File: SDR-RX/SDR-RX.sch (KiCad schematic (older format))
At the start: 44 parts, among them J1 Program, J2 Vin, J3 FM Antenna, J4 AM Antenna, J5 Conn_01x03_Male, Q1 S8050, Q2 S8050, SW1 Reset ESP, SW2 3V3 J5/J2, U1 Si4734-D60-GU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

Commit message: PCB layout for plastic enclosure
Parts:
- added H1, H2, H3, H4: MountingHole_Pad, MountingHole:MountingHole_2.7mm_Pad_Via, symbol Mechanical:MountingHole_Pad
- added J6: GPS, Connector_JST:JST_SH_BM04B-SRSS-TB_1x04-1MP_P1.00mm_Vertical, symbol Connector:Conn_01x04_Male
- J2: footprint Connector_JST:JST_XH_S2B-XH-A-1_1x02_P2.50mm_Horizontal -> Connector_JST:JST_XH_B2B-XH-A_1x02_P2.50mm_Vertical
- J4: footprint Connector_Coaxial:SMA_Samtec_SMA-J-P-X-ST-EM1_EdgeMount -> Connector_Coaxial:SMB_Jack_Vertical
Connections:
- net +3V3: now also J6.4 (Pin_4)
- net GND: now also J6.1 (Pin_1)
- net at U2.24 (IO2): now also J6.3 (Pin_3)
- net at U2.26 (IO4): now also J6.2 (Pin_2)
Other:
- note added: "ESP RX/GPS TX"
- note added: "ESP TX/GPS RX"
- moved on the sheet: J5
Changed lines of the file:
@@
 L power:GND #PWR0103
 U 1 1 5FE984E0
-P 6000 4200
-F 0 "#PWR0103" H 6000 3950 50  0001 C CNN
-F 1 "GND" H 6000 4000 50  0000 C CNN
-F 2 "" H 6000 4200 50  0001 C CNN
-F 3 "" H 6000 4200 50  0001 C CNN
-	1    6000 4200
+P 10050 1800
+F 0 "#PWR0103" H 10050 1550 50  0001 C CNN
+F 1 "GND" H 10050 1600 50  0000 C CNN
+F 2 "" H 10050 1800 50  0001 C CNN
+F 3 "" H 10050 1800 50  0001 C CNN
+	1    10050 1800
 	1    0    0    -1
 $EndComp
@@
 L power:GND1 #RFGND0102
 U 1 1 6006F2B5
-P 6200 4200
-F 0 "#RFGND0102" H 6200 3950 50  0001 C CNN
-F 1 "GND1" H 6100 4000 50  0000 L CNN
-F 2 "" H 6200 4200 50  0001 C CNN
-F 3 "" H 6200 4200 50  0001 C CNN
-	1    6200 4200
+P 10250 1800
+F 0 "#RFGND0102" H 10250 1550 50  0001 C CNN
+F 1 "GND1" H 10150 1600 50  0000 L CNN
+F 2 "" H 10250 1800 50  0001 C CNN
+F 3 "" H 10250 1800 50  0001 C CNN
+	1    10250 1800
 	1    0    0    -1
 $EndComp
@@
 F 0 "J2" H 5042 2225 50  0000 C CNN
 F 1 "Vin " H 5042 2316 50  0000 C CNN
-F 2 "Connector_JST:JST_XH_S2B-XH-A-1_1x02_P2.50mm_Horizontal" H 5150 2550 50  0001 C CNN
+F 2 "Connector_JST:JST_XH_B2B-XH-A_1x02_P2.50mm_Vertical" H 5150 2550 50  0001 C CNN
 F 3 "~" H 5150 2550 50  0001 C CNN
 	1    5150 2550
@@
 L Connector:Conn_01x03_Male J5
 U 1 1 6056D8FD
-P 6000 3700
-F 0 "J5" V 6062 3844 50  0000 L CNN
-F 1 "Conn_01x03_Male" V 6153 3844 50  0000 L CNN
-F 2 "Connector_PinHeader_2.54mm:PinHeader_1x03_P2.54mm_Vertical" H 6000 3700 50  0001 C CNN
-F 3 "~" H 6000 3700 50  0001 C CNN
-	1    6000 3700
+P 10050 1300
+F 0 "J5" V 10112 1444 50  0000 L CNN
+F 1 "Conn_01x03_Male" V 10203 1444 50  0000 L CNN
+F 2 "Connector_PinHeader_2.54mm:PinHeader_1x03_P2.54mm_Vertical" H 10050 1300 50  0001 C CNN
+F 3 "~" H 10050 1300 50  0001 C CNN
+	1    10050 1300
 	0    1    1    0
 $EndComp
 Wire Wire Line
-	5900 3900 6000 3900
-Wire Wire Line
-	6100 3900 6000 3900
-Connection ~ 6000 3900
+	9950 1500 10050 1500
+Wire Wire Line
+	10150 1500 10050 1500
+Connection ~ 10050 1500
 $Comp
 L Transistor_BJT:S8050 Q2
@@
 F 0 "J4" H 6850 5375 50  0000 L CNN
 F 1 "AM Antenna" H 6850 5284 50  0000 L CNN
-F 2 "Connector_Coaxial:SMA_Samtec_SMA-J-P-X-ST-EM1_EdgeMount" H 6750 5400 50  0001 C CNN
+F 2 "Connector_Coaxial:SMB_Jack_Vertical" H 6750 5400 50  0001 C CNN
 F 3 " ~" H 6750 5400 50  0001 C CNN
 	1    6750 5400
@@
 Connection ~ 7900 2050
 Wire Wire Line
-	6000 4200 6000 4150
-Wire Wire Line
-	6000 4150 6200 4150
-Wire Wire Line
-	6200 4150 6200 4200
-Wire Wire Line
-	6000 4150 6000 3900
-Connection ~ 6000 4150
+	10050 1800 10050 1750
+Wire Wire Line
+	10050 1750 10250 1750
+Wire Wire Line
+	10250 1750 10250 1800
+Wire Wire Line
+	10050 1750 10050 1500
+Connection ~ 10050 1750
 Wire Wire Line
 	5600 1000 5600 1150
@@
 Wire Wire Line
 	5600 1150 5600 1400
+$Comp
+L Mechanical:MountingHole_Pad H1
+U 1 1 6093FE17
+P 8500 1250
+F 0 "H1" H 8600 1299 50  0000 L CNN
+F 1 "MountingHole_Pad" H 8600 1208 50  0000 L CNN
+F 2 "MountingHole:MountingHole_2.7mm_Pad_Via" H 8500 1250 50  0001 C CNN
+F 3 "~" H 8500 1250 50  0001 C CNN
+	1    8500 1250
+	1    0    0    -1
+$EndComp
+$Comp
+L Mechanical:MountingHole_Pad H2
+U 1 1 6096087A
+P 8500 1550
+F 0 "H2" H 8600 1599 50  0000 L CNN
+F 1 "MountingHole_Pad" H 8600 1508 50  0000 L CNN
+F 2 "MountingHole:MountingHole_2.7mm_Pad_Via" H 8500 1550 50  0001 C CNN
+F 3 "~" H 8500 1550 50  0001 C CNN
+	1    8500 1550
+	1    0    0    -1
+$EndComp
+$Comp
+L Mechanical:MountingHole_Pad H3
+U 1 1 6096136C
+P 8500 1850
+F 0 "H3" H 8600 1899 50  0000 L CNN
+F 1 "MountingHole_Pad" H 8600 1808 50  0000 L CNN
+F 2 "MountingHole:MountingHole_2.7mm_Pad_Via" H 8500 1850 50  0001 C CNN
+F 3 "~" H 8500 1850 50  0001 C CNN
+	1    8500 1850
+	1    0    0    -1
+$EndComp
+$Comp
+L Mechanical:MountingHole_Pad H4
+U 1 1 60961E6D
+P 8500 2150
+F 0 "H4" H 8600 2199 50  0000 L CNN
+F 1 "MountingHole_Pad" H 8600 2108 50  0000 L CNN
+F 2 "MountingHole:MountingHole_2.7mm_Pad_Via" H 8500 2150 50  0001 C CNN
+F 3 "~" H 8500 2150 50  0001 C CNN
+	1    8500 2150
+	1    0    0    -1
+$EndComp
+$Comp
+L Connector:Conn_01x04_Male J6
+U 1 1 6078FB5B
+P 4000 3200
+F 0 "J6" H 4100 2850 50  0000 R CNN
+F 1 "GPS" H 3950 2850 50  0000 R CNN
+F 2 "Connector_JST:JST_SH_BM04B-SRSS-TB_1x04-1MP_P1.00mm_Vertical" H 4000 3200 50  0001 C CNN
+F 3 "https://datasheet.lcsc.com/szlcsc/2010160407_CJT-Changjiang-Connectors-A1002WR-S-4P_C239522.pdf" H 4000 3200 50  0001 C CNN
+F 4 "C239522" H 4000 3200 50  0001 C CNN "LCSC Part #"
+	1    4000 3200
+	-1   0    0    1
+$EndComp
+$Comp
+L power:GND #PWR0123
+U 1 1 607E0746
+P 3700 3400
+F 0 "#PWR0123" H 3700 3150 50  0001 C CNN
+F 1 "GND" H 3705 3227 50  0000 C CNN
+F 2 "" H 3700 3400 50  0001 C CNN
+F 3 "" H 3700 3400 50  0001 C CNN
+	1    3700 3400
+	1    0    0    -1
+$EndComp
+Wire Wire Line
+	3800 3300 3700 3300
+Wire Wire Line
+	3700 3300 3700 3400
+Wire Wire Line
+	2400 3200 3800 3200
+Wire Wire Line
+	2400 3000 3600 3000
+Wire Wire Line
+	3600 3000 3600 3100
+Wire Wire Line
+	3600 3100 3800 3100
+$Comp
+L power:+3V3 #PWR0124
+U 1 1 6080959D
+P 3700 2900
+F 0 "#PWR0124" H 3700 2750 50  0001 C CNN
+F 1 "+3V3" H 3715 3073 50  0000 C CNN
+F 2 "" H 3700 2900 50  0001 C CNN
+F 3 "" H 3700 2900 50  0001 C CNN
+	1    3700 2900
+	1    0    0    -1
+$EndComp
+Wire Wire Line
+	3800 3000 3700 3000
+Wire Wire Line
+	3700 3000 3700 2900
+Text Notes 4700 3200 2    50   ~ 0
+ESP RX/GPS TX
+Text Notes 4650 3100 2    50   ~ 0
+ESP TX/GPS RX
 $EndSCHEMATC

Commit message: changed footprint GPS header
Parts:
- D1: footprint Diode_SMD:D_MELF -> Diode_SMD:D_SOD-323F
- D4: footprint Diode_SMD:D_MELF -> Diode_SMD:D_SOD-123F
- TP5: value TestPoint -> +3V3
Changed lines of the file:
@@
 P 5700 1150
 F 0 "TP5" H 5642 1176 50  0000 R CNN
-F 1 "TestPoint" H 5642 1267 50  0000 R CNN
+F 1 "+3V3" H 5642 1267 50  0000 R CNN
 F 2 "TestPoint:TestPoint_Pad_D1.5mm" H 5900 1150 50  0001 C CNN
 F 3 "~" H 5900 1150 50  0001 C CNN
@@
 F 0 "D1" V 5804 2780 50  0000 L CNN
 F 1 "SM4007" V 5895 2780 50  0000 L CNN
-F 2 "Diode_SMD:D_MELF" H 5850 2525 50  0001 C CNN
-F 3 "1903051030_MDD-Jiangsu-Yutai-Elec-SM4007PL_C64898.pdf" H 5850 2700 50  0001 C CNN
+F 2 "Diode_SMD:D_SOD-323F" H 5850 2525 50  0001 C CNN
+F 3 "https://datasheet.lcsc.com/lcsc/1809301215_MDD-Microdiode-Electronics-SM4007PL_C64898.pdf" H 5850 2700 50  0001 C CNN
 F 4 "C64898" V 5850 2700 50  0001 C CNN "LCSC Part #"
 	1    5850 2700
@@
 F 0 "D4" V 7454 2130 50  0000 L CNN
 F 1 "SM4007" V 7545 2130 50  0000 L CNN
-F 2 "Diode_SMD:D_MELF" H 7500 1875 50  0001 C CNN
-F 3 "1903051030_MDD-Jiangsu-Yutai-Elec-SM4007PL_C64898.pdf" H 7500 2050 50  0001 C CNN
+F 2 "Diode_SMD:D_SOD-123F" H 7500 1875 50  0001 C CNN
+F 3 "https://datasheet.lcsc.com/lcsc/1809301215_MDD-Microdiode-Electronics-SM4007PL_C64898.pdf" H 7500 2050 50  0001 C CNN
 F 4 "C64898" V 7500 2050 50  0001 C CNN "LCSC Part #"
 	1    7500 2050

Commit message: Added BOM and schematics.pdf
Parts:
- C3: LCSC Part # C21117 -> C21117
- SW2: Field4 C160876 -> (none); LCSC Part # (none) -> C160876
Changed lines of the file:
@@
 F 2 "Capacitor_SMD:C_0603_1608Metric_Pad1.08x0.95mm_HandSolder" H 2038 6800 50  0001 C CNN
 F 3 "https://datasheet.lcsc.com/szlcsc/Samsung-Electro-Mechanics-CL10B333KB8NNNC_C21117.pdf" H 2000 6950 50  0001 C CNN
-F 4 " C21117" H 2000 6950 50  0001 C CNN "LCSC Part #"
+F 4 "C21117" H 2000 6950 50  0001 C CNN "LCSC Part #"
 	1    2000 6950
 	1    0    0    -1
@@
 F 1 "Fuse_1A" H 5650 2544 50  0000 C CNN
 F 2 "Fuse:Fuse_1206_3216Metric_Pad1.42x1.75mm_HandSolder" H 5650 2450 50  0001 C CNN
-F 3 "Shenzhen-lanson-Elec-12H1100C_C182308.pdf" H 5650 2450 50  0001 C CNN
+F 3 "https://datasheet.lcsc.com/lcsc/1808301741_Shenzhen-lanson-Elec-12H1100C_C182308.pdf" H 5650 2450 50  0001 C CNN
 F 4 "C182308" H 5650 2450 50  0001 C CNN "LCSC Part #"
 	1    5650 2450
@@
 F 1 "10uF" H 6900 2600 50  0000 L CNN
 F 2 "Capacitor_SMD:C_1206_3216Metric_Pad1.33x1.80mm_HandSolder" H 7138 2550 50  0001 C CNN
-F 3 "Samsung-Electro-Mechanics-CL31A106KBHNNNE_C13585.pdf" H 7100 2700 50  0001 C CNN
+F 3 "https://datasheet.lcsc.com/szlcsc/Samsung-Electro-Mechanics-CL31A106KBHNNNE_C13585.pdf" H 7100 2700 50  0001 C CNN
 F 4 "C13585" H 7100 2700 50  0001 C CNN "LCSC Part #"
 	1    7100 2700
@@
 F 1 "10uF" H 6400 2600 50  0000 L CNN
 F 2 "Capacitor_SMD:C_1206_3216Metric_Pad1.33x1.80mm_HandSolder" H 6638 2550 50  0001 C CNN
-F 3 "Samsung-Electro-Mechanics-CL31A106KBHNNNE_C13585.pdf" H 6600 2700 50  0001 C CNN
+F 3 "https://datasheet.lcsc.com/szlcsc/Samsung-Electro-Mechanics-CL31A106KBHNNNE_C13585.pdf" H 6600 2700 50  0001 C CNN
 F 4 "C13585" H 6600 2700 50  0001 C CNN "LCSC Part #"
 	1    6600 2700
@@
 F 1 "10uF" H 1200 2100 50  0000 L CNN
 F 2 "Capacitor_SMD:C_1206_3216Metric_Pad1.33x1.80mm_HandSolder" H 1438 2050 50  0001 C CNN
-F 3 "Samsung-Electro-Mechanics-CL31A106KBHNNNE_C13585.pdf" H 1400 2200 50  0001 C CNN
+F 3 "https://datasheet.lcsc.com/szlcsc/Samsung-Electro-Mechanics-CL31A106KBHNNNE_C13585.pdf" H 1400 2200 50  0001 C CNN
 F 4 "C13585" H 1400 2200 50  0001 C CNN "LCSC Part #"
 	1    1400 2200
@@
 F 1 "10uF" H 4250 1350 50  0000 L CNN
 F 2 "Capacitor_SMD:C_1206_3216Metric_Pad1.33x1.80mm_HandSolder" H 4238 1350 50  0001 C CNN
-F 3 "Samsung-Electro-Mechanics-CL31A106KBHNNNE_C13585.pdf" H 4200 1500 50  0001 C CNN
+F 3 "https://datasheet.lcsc.com/szlcsc/Samsung-Electro-Mechanics-CL31A106KBHNNNE_C13585.pdf" H 4200 1500 50  0001 C CNN
 F 4 "C13585" H 4200 1500 50  0001 C CNN "LCSC Part #"
 	1    4200 1500
@@
 F 2 "Button_Switch_SMD:SW_SPDT_CK-JS102011SAQN" H 5100 1400 50  0001 C CNN
 F 3 "https://datasheet.lcsc.com/szlcsc/1809041640_ALPSALPINE-SSSS710607_C160876.pdf" H 5100 1400 50  0001 C CNN
-F 4 "C160876" H 5100 1400 50  0001 C CNN "Field4"
+F 4 "C160876" H 5100 1400 50  0001 C CNN "LCSC Part #"
 	1    5100 1400
 	-1   0    0    1

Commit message: changed footprint D1 & D4 due to assembly objection
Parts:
- D1: footprint Diode_SMD:D_SOD-323F -> Diode_SMD:D_1206_3216Metric_Pad1.42x1.75mm_HandSolder
- D4: footprint Diode_SMD:D_SOD-123F -> Diode_SMD:D_1206_3216Metric_Pad1.42x1.75mm_HandSolder
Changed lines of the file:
@@
 F 0 "D1" V 5804 2780 50  0000 L CNN
 F 1 "SM4007" V 5895 2780 50  0000 L CNN
-F 2 "Diode_SMD:D_SOD-323F" H 5850 2525 50  0001 C CNN
+F 2 "Diode_SMD:D_1206_3216Metric_Pad1.42x1.75mm_HandSolder" H 5850 2525 50  0001 C CNN
 F 3 "https://datasheet.lcsc.com/lcsc/1809301215_MDD-Microdiode-Electronics-SM4007PL_C64898.pdf" H 5850 2700 50  0001 C CNN
 F 4 "C64898" V 5850 2700 50  0001 C CNN "LCSC Part #"
@@
 F 0 "D4" V 7454 2130 50  0000 L CNN
 F 1 "SM4007" V 7545 2130 50  0000 L CNN
-F 2 "Diode_SMD:D_SOD-123F" H 7500 1875 50  0001 C CNN
+F 2 "Diode_SMD:D_1206_3216Metric_Pad1.42x1.75mm_HandSolder" H 7500 1875 50  0001 C CNN
 F 3 "https://datasheet.lcsc.com/lcsc/1809301215_MDD-Microdiode-Electronics-SM4007PL_C64898.pdf" H 7500 2050 50  0001 C CNN
 F 4 "C64898" V 7500 2050 50  0001 C CNN "LCSC Part #"

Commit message: moved Prog-Vin1 switch closer to pcb edge, changed anotation GND1 of GND TP
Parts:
- Prog-Vin1: renamed from SW2; value 3V3 J5/J2 -> SW2
- Reset1: renamed from SW1; value Reset ESP -> SW1
- renumbered J5 to GND
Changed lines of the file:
@@
 $EndComp
 $Comp
-L Connector:Conn_01x03_Male J5
+L Connector:Conn_01x03_Male GND
 U 1 1 6056D8FD
 P 10050 1300
-F 0 "J5" V 10112 1444 50  0000 L CNN
+F 0 "GND" V 10112 1444 50  0000 L CNN
 F 1 "Conn_01x03_Male" V 10203 1444 50  0000 L CNN
 F 2 "Connector_PinHeader_2.54mm:PinHeader_1x03_P2.54mm_Vertical" H 10050 1300 50  0001 C CNN
@@
 GND
 $Comp
-L Switch:SW_DPST_x2 SW1
+L Switch:SW_DPST_x2 Reset1
 U 1 1 60989D58
 P 1000 2050
-F 0 "SW1" H 1000 2000 50  0000 C CNN
-F 1 "Reset ESP" H 1000 2200 50  0000 C CNN
+F 0 "Reset1" H 1000 2300 50  0000 C CNN
+F 1 "SW1" H 1000 2200 50  0000 C CNN
 F 2 "Button_Switch_SMD:SW_SPST_B3SL-1002P" H 1000 2350 50  0001 C CNN
 F 3 "https://datasheet.lcsc.com/szlcsc/XKB-TS-1187A-C-E-A_C318887.pdf" H 1000 2350 50  0001 C CNN
@@
 	3200 1300 3200 1200
 $Comp
-L Switch:SW_SPDT SW2
+L Switch:SW_SPDT Prog-Vin1
 U 1 1 60790519
 P 5100 1400
-F 0 "SW2" H 5100 1075 50  0000 C CNN
-F 1 "3V3 J5/J2" H 5100 1166 50  0000 C CNN
+F 0 "Prog-Vin1" H 5100 1075 50  0000 C CNN
+F 1 "SW2" H 5100 1166 50  0000 C CNN
 F 2 "Button_Switch_SMD:SW_SPDT_CK-JS102011SAQN" H 5100 1400 50  0001 C CNN
 F 3 "https://datasheet.lcsc.com/szlcsc/1809041640_ALPSALPINE-SSSS710607_C160876.pdf" H 5100 1400 50  0001 C CNN

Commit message: changed Designator J5 to Program1 to avoid BPM/CPL missmatch on SMT assembly
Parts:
- GND1: renamed from GND; value Conn_01x03_Male -> GND TP
- Program1: renamed from J1; value Program -> J1
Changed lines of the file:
@@
 	1800 2000 1800 2600
 $Comp
-L Connector:Conn_01x07_Female J1
+L Connector:Conn_01x07_Female Program1
 U 1 1 6032807C
 P 3500 1000
-F 0 "J1" V 3750 900 50  0000 R CNN
-F 1 "Program" V 3750 1300 50  0000 R CNN
+F 0 "Program1" V 3750 900 50  0000 R CNN
+F 1 "J1" V 3750 1300 50  0000 R CNN
 F 2 "Connector_JST:JST_XH_S7B-XH-A-1_1x07_P2.50mm_Horizontal" H 3500 1000 50  0001 C CNN
 F 3 "" H 3500 1000 50  0001 C CNN
@@
 $EndComp
 $Comp
-L Connector:Conn_01x03_Male GND
+L Connector:Conn_01x03_Male GND1
 U 1 1 6056D8FD
 P 10050 1300
-F 0 "GND" V 10112 1444 50  0000 L CNN
-F 1 "Conn_01x03_Male" V 10203 1444 50  0000 L CNN
+F 0 "GND1" V 10112 1444 50  0000 L CNN
+F 1 "GND TP" V 10203 1444 50  0000 L CNN
 F 2 "Connector_PinHeader_2.54mm:PinHeader_1x03_P2.54mm_Vertical" H 10050 1300 50  0001 C CNN
 F 3 "~" H 10050 1300 50  0001 C CNN

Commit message: reversed remaining value/designator of all connectors
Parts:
- FM: renamed from J3; value FM Antenna -> J3
- GPS: renamed from J6; value GPS -> J6
- SW-AM: renamed from J4; value AM Antenna -> J4
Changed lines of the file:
@@
 F 2 "Package_SO:SSOP-24_3.9x8.7mm_P0.635mm" H 4350 5600 50  0001 L CNN
 F 3 "http://www.silabs.com/Support%20Documents/TechnicalDocs/Si4730-31-34-35-D60.pdf" H 4150 5300 50  0001 C CNN
+F 4 "" H 4100 6300 50  0001 C CNN "LCSC Part #"
 	1    4100 6300
 	1    0    0    -1
@@
 Connection ~ 3100 6100
 $Comp
-L Connector:Conn_Coaxial J4
+L Connector:Conn_Coaxial SW-AM
 U 1 1 6101FE8D
 P 6750 5400
-F 0 "J4" H 6850 5375 50  0000 L CNN
-F 1 "AM Antenna" H 6850 5284 50  0000 L CNN
+F 0 "SW-AM" H 6850 5375 50  0000 L CNN
+F 1 "J4" H 6850 5284 50  0000 L CNN
 F 2 "Connector_Coaxial:SMB_Jack_Vertical" H 6750 5400 50  0001 C CNN
 F 3 " ~" H 6750 5400 50  0001 C CNN
@@
 $EndComp
 $Comp
-L Connector:Conn_Coaxial J3
+L Connector:Conn_Coaxial FM
 U 1 1 6010BDF0
 P 6250 6600
-F 0 "J3" H 6350 6575 50  0000 L CNN
-F 1 "FM Antenna" H 6350 6484 50  0000 L CNN
+F 0 "FM" H 6350 6575 50  0000 L CNN
+F 1 "J3" H 6350 6484 50  0000 L CNN
 F 2 "Connector_Coaxial:SMA_Samtec_SMA-J-P-X-ST-EM1_EdgeMount" H 6250 6600 50  0001 C CNN
 F 3 " ~" H 6250 6600 50  0001 C CNN
@@
 $EndComp
 $Comp
-L Connector:Conn_01x04_Male J6
+L Connector:Conn_01x04_Male GPS
 U 1 1 6078FB5B
 P 4000 3200
-F 0 "J6" H 4100 2850 50  0000 R CNN
-F 1 "GPS" H 3950 2850 50  0000 R CNN
+F 0 "GPS" H 4100 2850 50  0000 R CNN
+F 1 "J6" H 3950 2850 50  0000 R CNN
 F 2 "Connector_JST:JST_SH_BM04B-SRSS-TB_1x04-1MP_P1.00mm_Vertical" H 4000 3200 50  0001 C CNN
 F 3 "https://datasheet.lcsc.com/szlcsc/2010160407_CJT-Changjiang-Connectors-A1002WR-S-4P_C239522.pdf" H 4000 3200 50  0001 C CNN

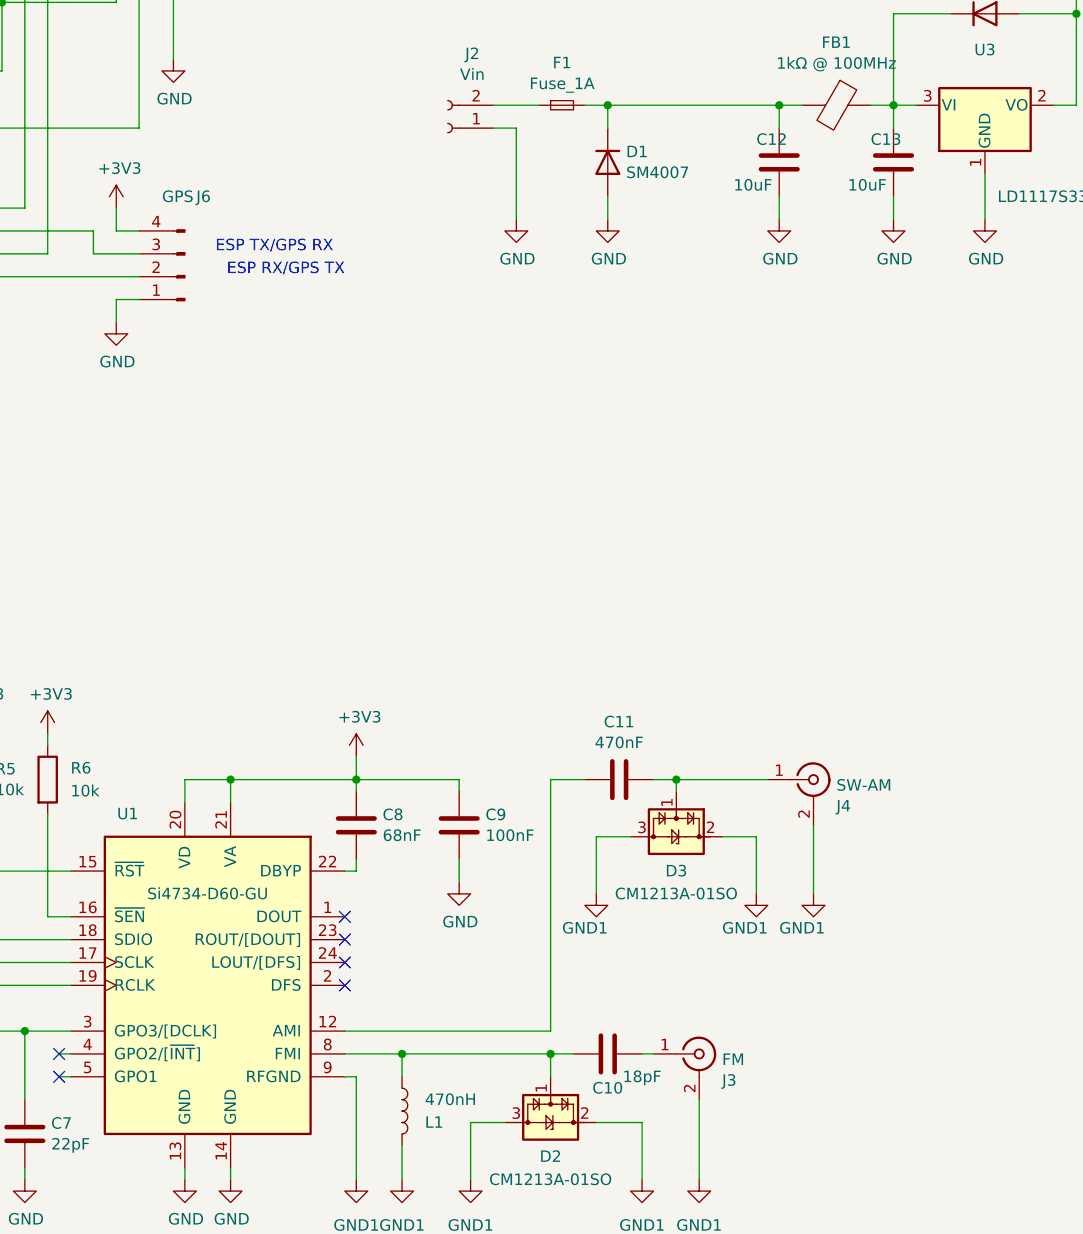
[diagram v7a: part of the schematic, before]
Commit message: adapted footprint of GPS1/J6 to real footprint of SMT assembly, created hb9gvd.pretty directory
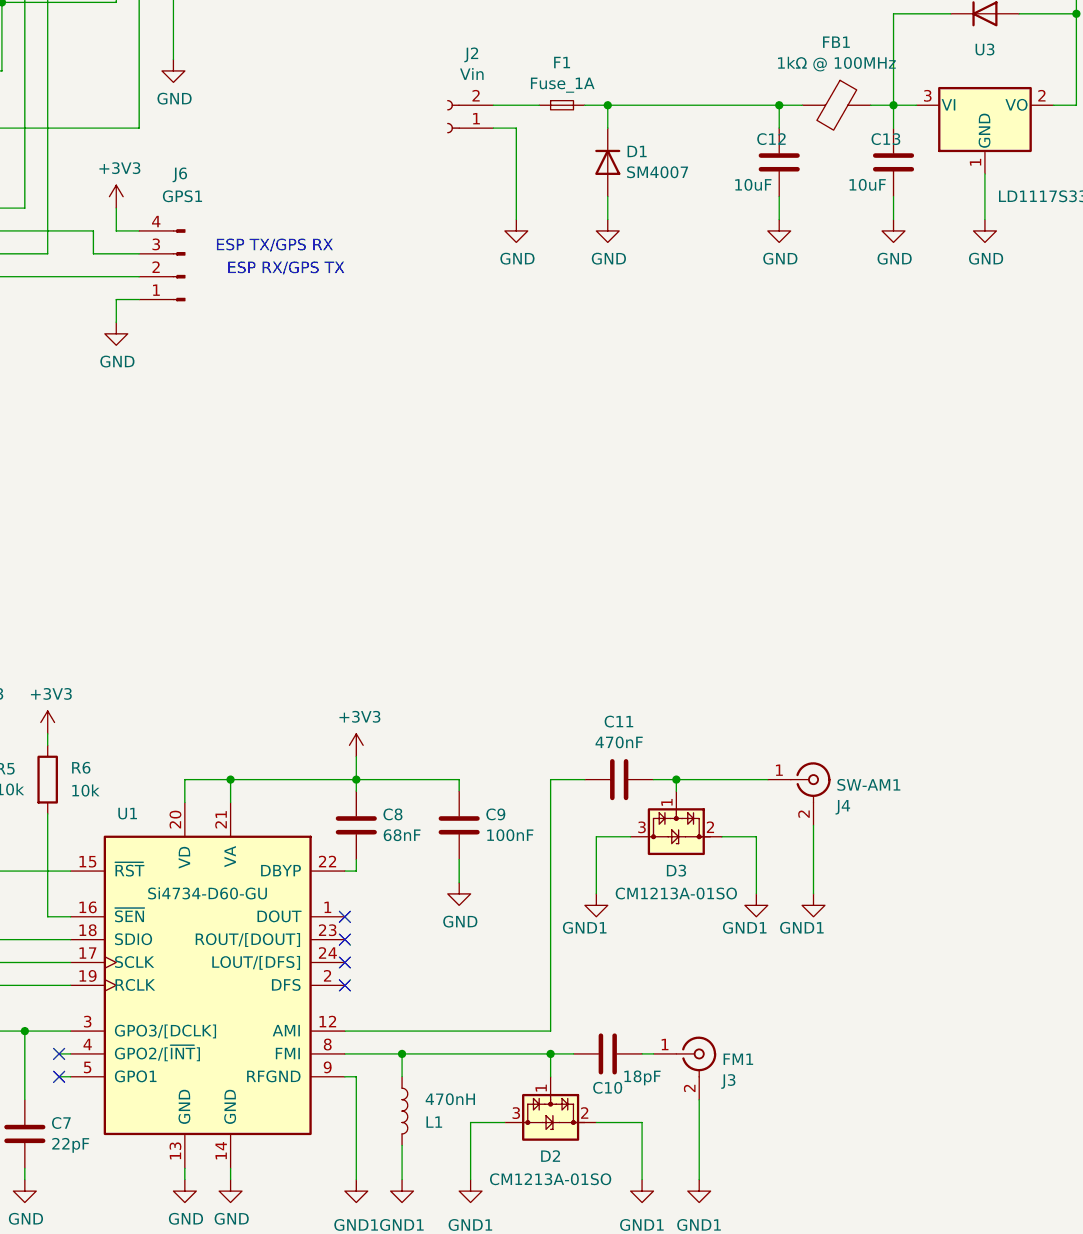
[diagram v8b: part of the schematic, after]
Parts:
- GPS1: renamed from GPS; footprint Connector_JST:JST_SH_BM04B-SRSS-TB_1x04-1MP_P1.00mm_Vertical -> hb9gvd:JST_SH_BM04B-SRSS-TB_1x04-1MP_P1.00mm_Vertical-GPS
- renumbered FM to FM1, SW-AM to SW-AM1
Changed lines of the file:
@@
 Connection ~ 3100 6100
 $Comp
-L Connector:Conn_Coaxial SW-AM
+L Connector:Conn_Coaxial SW-AM1
 U 1 1 6101FE8D
 P 6750 5400
-F 0 "SW-AM" H 6850 5375 50  0000 L CNN
+F 0 "SW-AM1" H 6850 5375 50  0000 L CNN
 F 1 "J4" H 6850 5284 50  0000 L CNN
 F 2 "Connector_Coaxial:SMB_Jack_Vertical" H 6750 5400 50  0001 C CNN
@@
 $EndComp
 $Comp
-L Connector:Conn_Coaxial FM
+L Connector:Conn_Coaxial FM1
 U 1 1 6010BDF0
 P 6250 6600
-F 0 "FM" H 6350 6575 50  0000 L CNN
+F 0 "FM1" H 6350 6575 50  0000 L CNN
 F 1 "J3" H 6350 6484 50  0000 L CNN
 F 2 "Connector_Coaxial:SMA_Samtec_SMA-J-P-X-ST-EM1_EdgeMount" H 6250 6600 50  0001 C CNN
@@
 $EndComp
 $Comp
-L Connector:Conn_01x04_Male GPS
+L Connector:Conn_01x04_Male GPS1
 U 1 1 6078FB5B
 P 4000 3200
-F 0 "GPS" H 4100 2850 50  0000 R CNN
-F 1 "J6" H 3950 2850 50  0000 R CNN
-F 2 "Connector_JST:JST_SH_BM04B-SRSS-TB_1x04-1MP_P1.00mm_Vertical" H 4000 3200 50  0001 C CNN
+F 0 "GPS1" H 4100 2850 50  0000 R CNN
+F 1 "J6" H 4050 2750 50  0000 R CNN
+F 2 "hb9gvd:JST_SH_BM04B-SRSS-TB_1x04-1MP_P1.00mm_Vertical-GPS" H 4000 3200 50  0001 C CNN
 F 3 "https://datasheet.lcsc.com/szlcsc/2010160407_CJT-Changjiang-Connectors-A1002WR-S-4P_C239522.pdf" H 4000 3200 50  0001 C CNN
 F 4 "C239522" H 4000 3200 50  0001 C CNN "LCSC Part #"
